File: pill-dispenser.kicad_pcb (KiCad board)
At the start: 2 copper layers, 50 x 50 mm, 34 parts, among them Q1 AO3401A, Q2 FS8205A, U1 MT3608, U3 TP4056-42-ESOP8, U4 DW01A

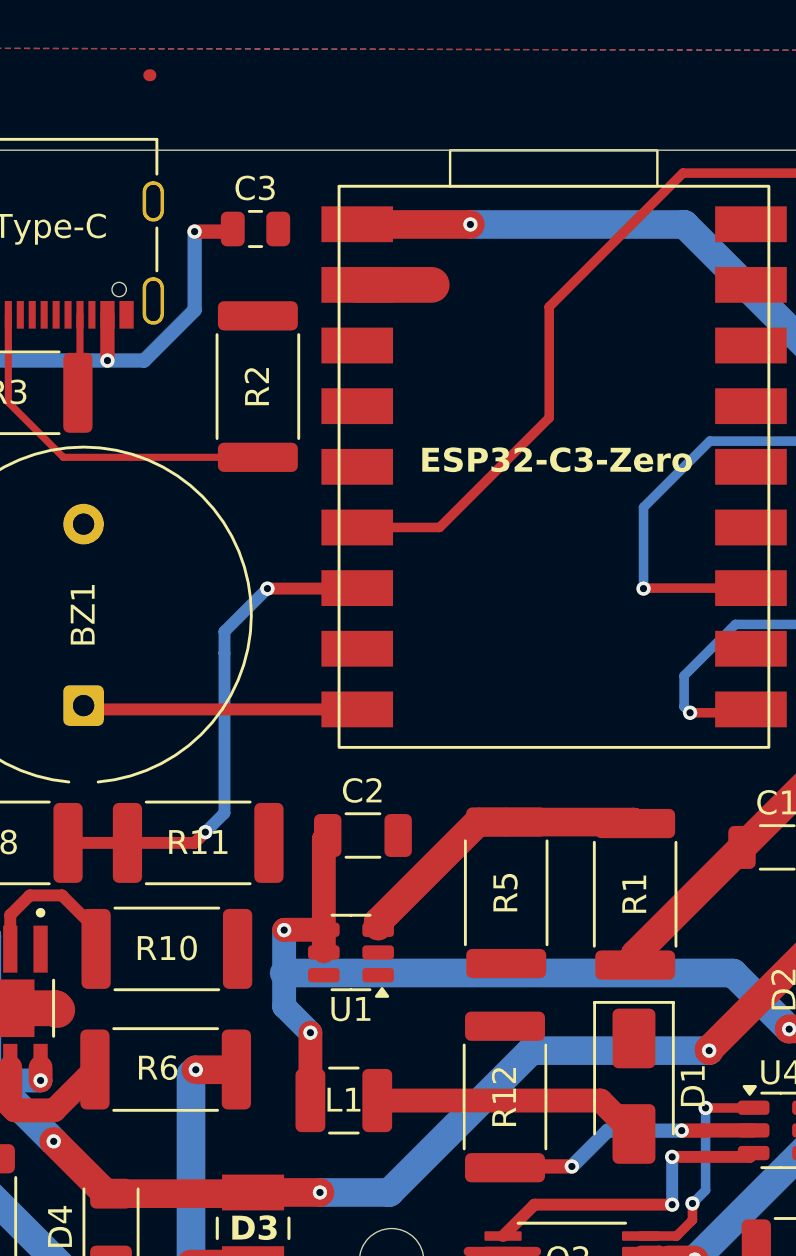
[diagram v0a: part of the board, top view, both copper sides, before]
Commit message: Fixed errors in PCB layout
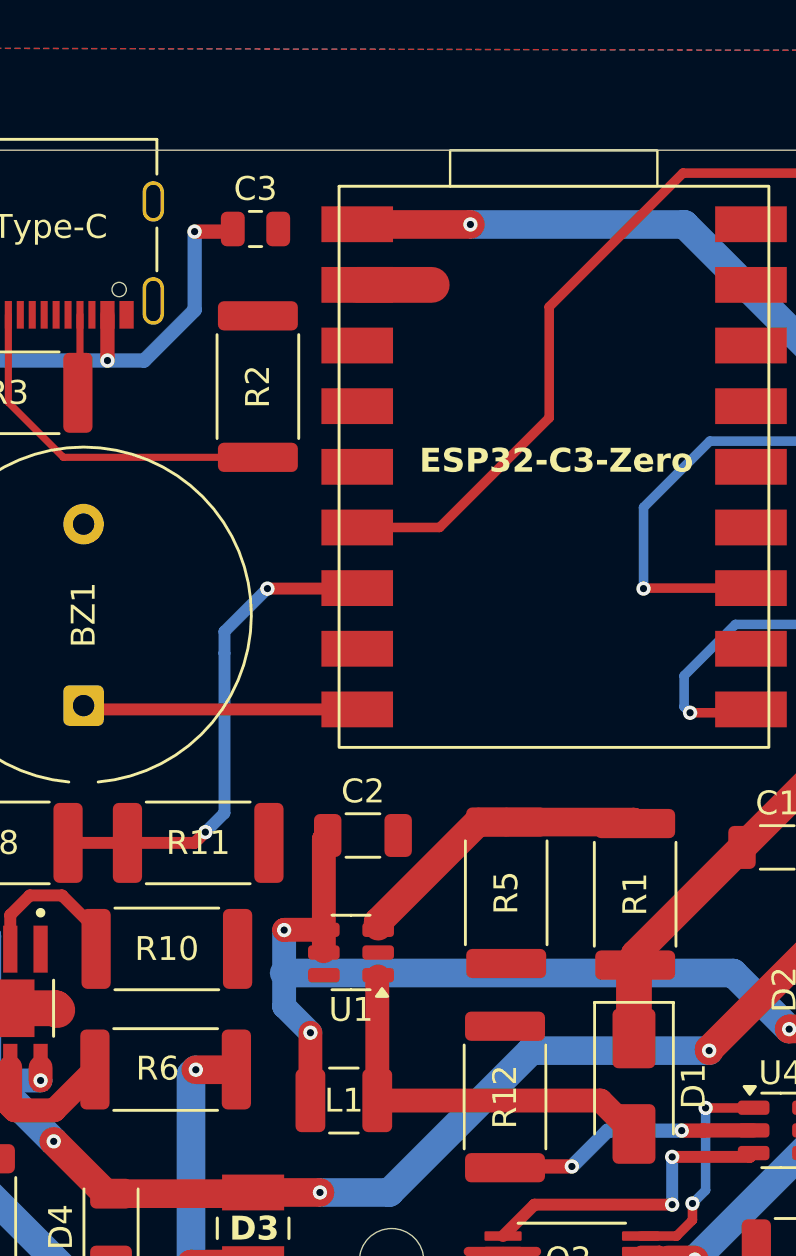
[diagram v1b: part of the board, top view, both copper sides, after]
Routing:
- net Net-(D1-A): track 11.3 -> 16.5 mm
- net +5V: track 61.4 -> 64.5 mm
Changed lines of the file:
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@@
 	(generator_version "9.0")
 	(general
-		(thickness 1.6)
+		(thickness 2.09)
 		(legacy_teardrops no)
 	)
@@
 			(layer "F.SilkS"
 				(type "Top Silk Screen")
+				(color "Green")
 			)
 			(layer "F.Paste"
@@
 			(layer "dielectric 1"
 				(type "core")
-				(thickness 1.51)
+				(color "FR4 natural")
+				(thickness 2)
 				(material "FR4")
 				(epsilon_r 4.5)
@@
 			(layer "B.SilkS"
 				(type "Bottom Silk Screen")
+				(color "Green")
 			)
 			(copper_finish "None")
@@
 			)
 		)
-		(property ki_fp_filters "*Buzzer*")
 		(sheetname "/")
 		(sheetfile "pill-dispenser.kicad_sch")
@@
 			)
 		)
-		(property ki_fp_filters "*SO*3.9x4.*P1.27mm*EP2.4*x3.3*mm*")
 		(sheetname "/")
 		(sheetfile "pill-dispenser.kicad_sch")
@@
 	)
 	(segment
-		(start 114.6 77.95)
-		(end 114.55 77.95)
-		(width 0.5)
-		(layer "F.Cu")
-		(net 0)
-	)
-	(segment
 		(start 123.26 104.51)
 		(end 111.96 104.51)
@@
 	)
 	(segment
+		(start 134.85 115.265)
+		(end 134.9 115.215)
+		(width 1.5)
+		(layer "F.Cu")
+		(net 3)
+	)
+	(segment
+		(start 134.85 118.29)
+		(end 134.85 115.265)
+		(width 1.5)
+		(layer "F.Cu")
+		(net 3)
+	)
+	(segment
 		(start 139.375 110.29)
 		(end 143.215 106.45)
@@
 	)
 	(segment
+		(start 124.1 115.7285)
+		(end 124.1375 115.691)
+		(width 1)
+		(layer "F.Cu")
+		(net 8)
+	)
+	(segment
 		(start 134.85 122.29)
 		(end 133.45 120.89)
@@
 		(width 1)
 		(layer "F.Cu")
+		(net 8)
+	)
+	(segment
+		(start 124.1 120.89)
+		(end 124.1 115.7285)
+		(width 1)
+		(layer "F.Cu")

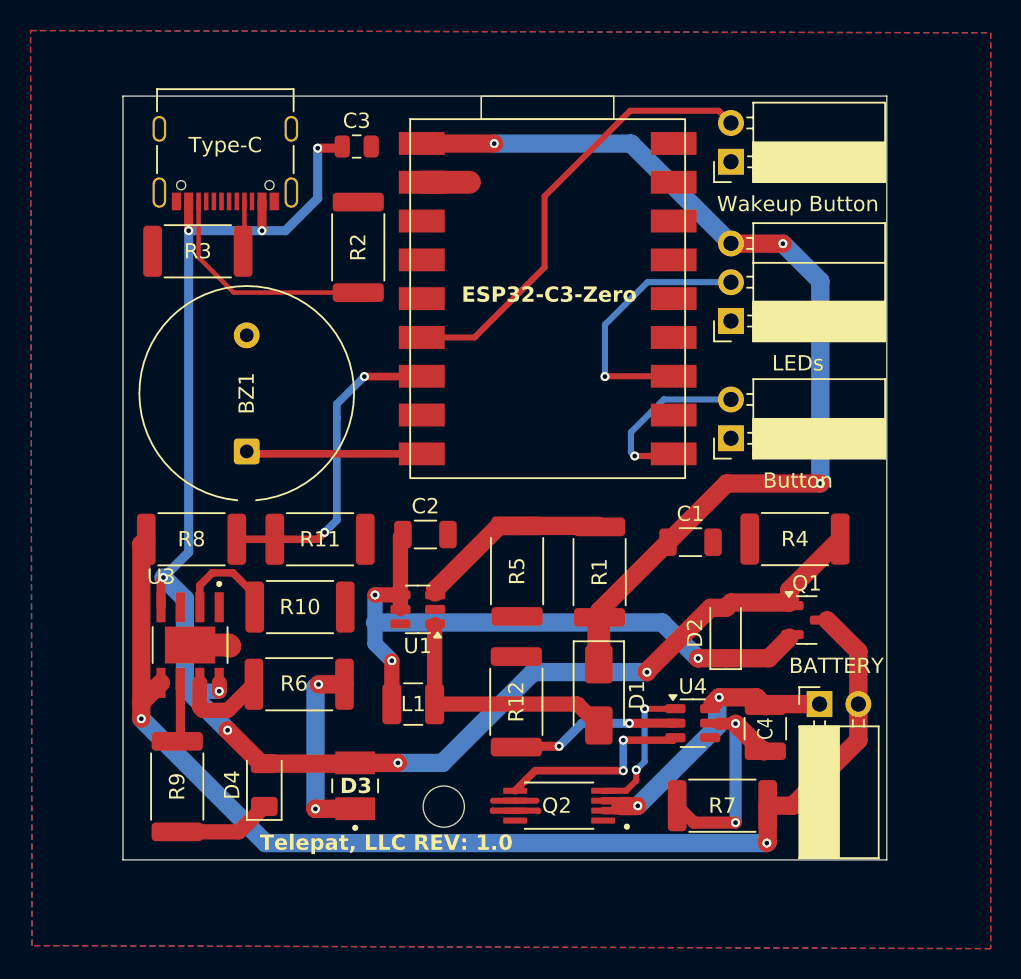
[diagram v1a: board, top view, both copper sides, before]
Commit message: Updated PCB to REV1.1 version
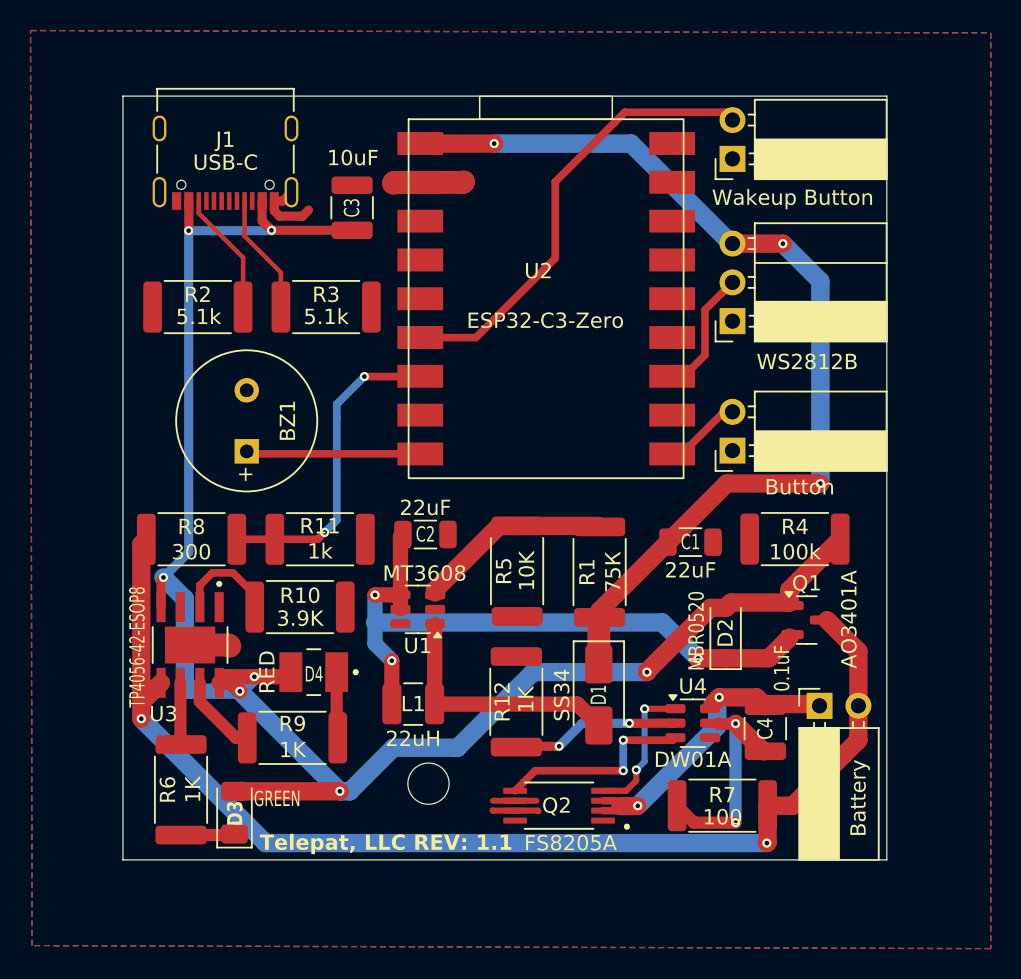
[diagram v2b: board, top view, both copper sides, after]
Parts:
- removed BATTERY: BAT, Connector_PinSocket_2.54mm:PinSocket_1x02_P2.54mm_Horizontal
- removed Button: Button, Connector_PinSocket_2.54mm:PinSocket_1x02_P2.54mm_Horizontal
- removed ESP32-C3-Zero: ESP32-C3-Zero, waveshare-esp32:Waveshare-ESP32-C3-Zero
- removed LEDs: WS2812B, Connector_PinSocket_2.54mm:PinSocket_1x03_P2.54mm_Horizontal
- removed Type-C: USB-C, Connector_USB:USB_C_Receptacle_Palconn_UTC16-G
- removed Wakeup Button: Wakeup Button, Connector_PinSocket_2.54mm:PinSocket_1x02_P2.54mm_Horizontal
- added J1: USB-C, Connector_USB:USB_C_Receptacle_Palconn_UTC16-G, F.Cu at (110.4, 85.5)
- added J2: Battery, Connector_PinSocket_2.54mm:PinSocket_1x02_P2.54mm_Horizontal, F.Cu at (149.3, 121.0)
- added J3: WS2812B, Connector_PinSocket_2.54mm:PinSocket_1x03_P2.54mm_Horizontal, F.Cu at (143.6, 95.8)
- added J4: Button, Connector_PinSocket_2.54mm:PinSocket_1x02_P2.54mm_Horizontal, F.Cu at (143.6, 104.3)
- added J5: Wakeup Button, Connector_PinSocket_2.54mm:PinSocket_1x02_P2.54mm_Horizontal, F.Cu at (143.6, 85.2)
- added U2: ESP32-C3-Zero, waveshare-esp32:Waveshare-ESP32-C3-Zero, F.Cu at (130.9, 94.1)
- BZ1: footprint Buzzer_Beeper:Indicator_PUI_AI-1440-TWT-24V-2-R -> Buzzer_Beeper:MagneticBuzzer_PUI_AT-0927-TT-6-R
- C3: footprint Capacitor_SMD:C_0805_2012Metric -> Capacitor_SMD:C_1210_3225Metric
- D3: value RED -> GREEN; footprint LS-T676-Q1R2-1-Z:LED_LG_T671-L2N1-1-Z -> LED_SMD:LED_1206_3216Metric
- D4: value GREEN -> RED; footprint LED_SMD:LED_1206_3216Metric -> LS-T676-Q1R2-1-Z:LED_LG_T671-L2N1-1-Z
- moved R2 11.2 mm to (108.6, 94.9), turned to 0 degrees
- moved R6 10.4 mm to (107.5, 126.5), turned to 90 degrees
- moved R3 9.16 mm to (117.0, 94.9), turned to 180 degrees
- moved R9 8.20 mm to (114.8, 123.1), turned to 180 degrees
- moved D3 8.09 mm to (111.0, 128.0)
- moved D4 8.07 mm to (116.2, 118.8), turned to 180 degrees
- moved C3 4.02 mm to (118.7, 88.4), turned to 90 degrees
- moved REF** 1.80 mm to (123.7, 126.1)
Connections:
- R6 pad 2: Net-(U3-~{CHRG}) -> Net-(U3-~{STDBY})
- R9 pad 2: Net-(U3-~{STDBY}) -> Net-(U3-~{CHRG})
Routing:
- net VUSB: track 105.7 -> 115.9 mm, vias 8 -> 7
- net /LED_STRIP: track 17.3 -> 8.23 mm, vias 1 -> 0
- net Net-(D3-K): track 12.5 -> 3.53 mm, vias 2 -> 0
- net Net-(J1-CC2): track 15.1 -> 8.14 mm
- net /BUTTON: track 11.7 -> 5.29 mm, vias 1 -> 0
- net GND: track 11.6 -> 17.7 mm
- net Net-(J1-CC1): track 3.30 -> 7.92 mm
- net Net-(D4-K): track 6.39 -> 4.33 mm
- net Net-(U3-~{CHRG}): track 5.94 -> 5.32 mm
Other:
- board text added: "Telepat, LLC REV: 1.1"
- board text removed: "Telepat, LLC REV: 1.0"
